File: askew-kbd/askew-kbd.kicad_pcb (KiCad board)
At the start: 2 copper layers, 166.1 x 111 mm, 45 parts, among them SW1 SW_PUSH, SW10 SW_PUSH, SW11 SW_PUSH, SW12 SW_PUSH, SW13 SW_PUSH, SW14 SW_PUSH, SW15 SW_PUSH, SW16 SW_PUSH, SW17 SW_PUSH, SW18 SW_PUSH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

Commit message: unrouted base
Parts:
- U1: footprint kbd:ProMicro_v2 -> keyboard_reversible:ProMicro_unrouted
- moved D22 9.83 mm to (192.2, 137.8), turned to 60 degrees
- moved U1 1.35 mm to (205.0, 79.6), turned to -95 degrees
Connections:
- U1 pad 10: unconnected-(U1-Pad10) -> home
- U1 pad 11: unconnected-(U1-Pad11) -> bottom
- U1 pad 12: unconnected-(U1-Pad12) -> thumb
- U1 pad 21: unconnected-(U1-Pad21) -> VCC
- U1 pad 22: unconnected-(U1-Pad22) -> reset
- U1 pad 23: unconnected-(U1-Pad23) -> GND
- U1 pad 3: unconnected-(U1-Pad3) -> GND
- U1 pad 4: unconnected-(U1-Pad4) -> GND
- U1 pad 9: unconnected-(U1-Pad9) -> top
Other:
- board size 166.1 x 111 mm -> 157.1 x 109 mm

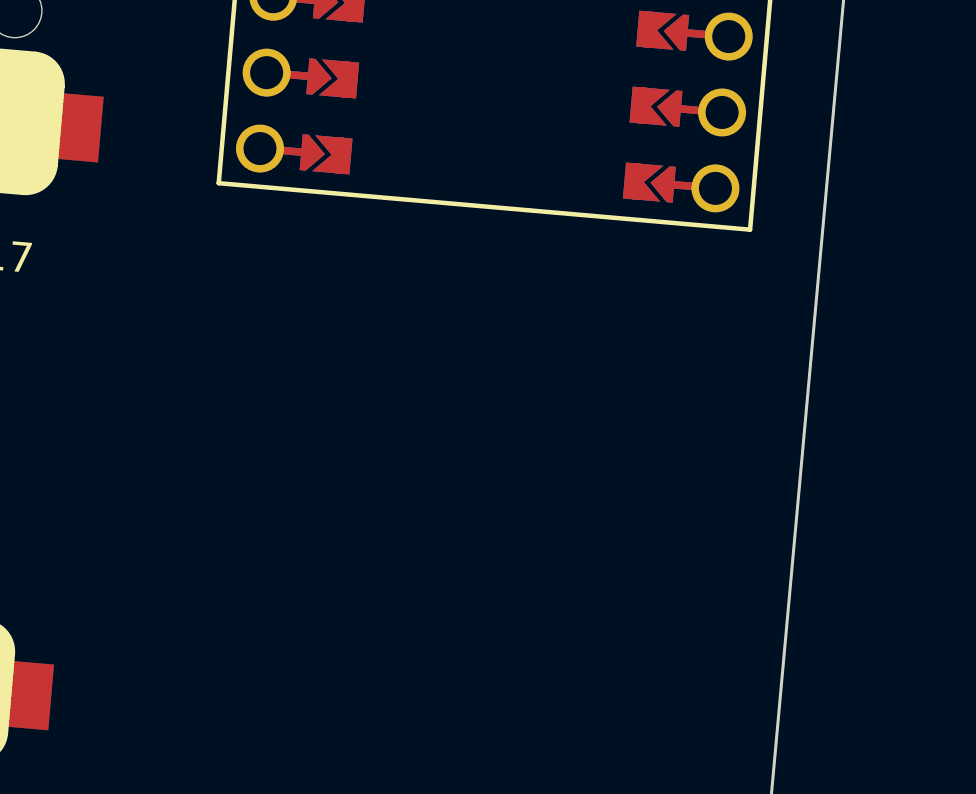
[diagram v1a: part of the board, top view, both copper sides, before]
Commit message: trrs and reset switch
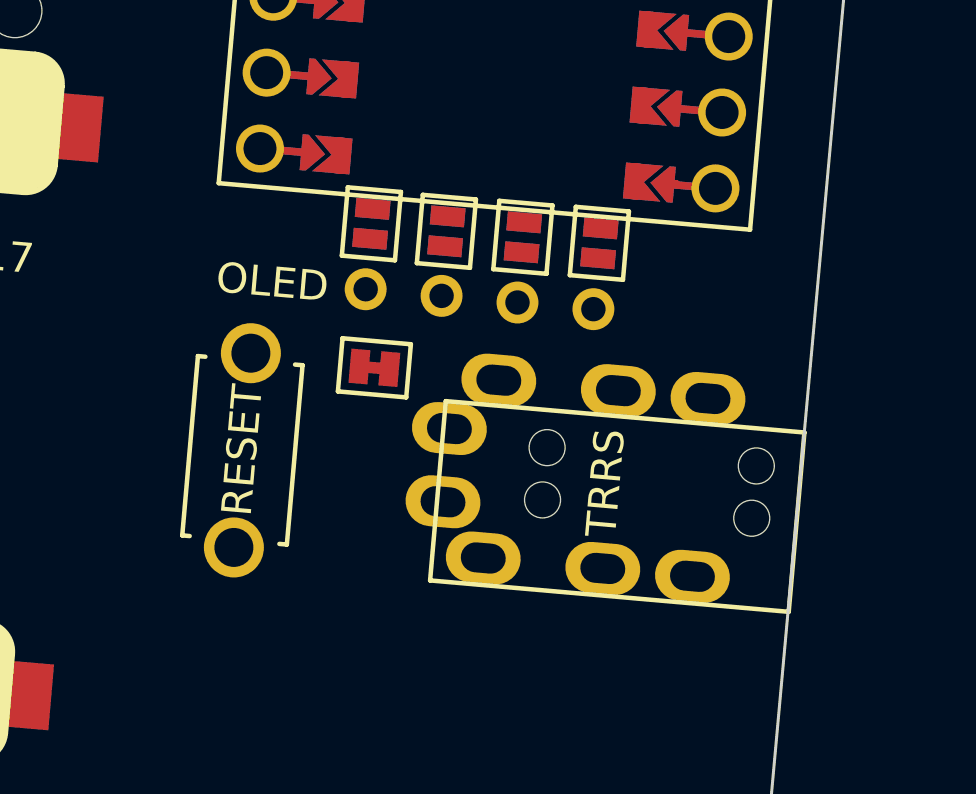
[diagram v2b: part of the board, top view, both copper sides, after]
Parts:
- added J1: OLED, kbd:OLED_v2, F.Cu at (203.5, 97.9)
- added J2: MJ-4PP-9, kbd:MJ-4PP-9, F.Cu at (214.1, 105.3)
- added JP1: , kbd:Jumper, F.Cu at (207.5, 96.0)
- added JP2: , kbd:Jumper, F.Cu at (204.9, 95.8)
- added JP3: , kbd:Jumper, F.Cu at (202.4, 95.6)
- added JP4: , kbd:Jumper, F.Cu at (199.9, 95.3)
- added JP5: , kbd:Jumper, B.Cu at (207.5, 96.0)
- added JP6: , kbd:Jumper, B.Cu at (204.9, 95.8)
- added JP7: , kbd:Jumper, B.Cu at (202.4, 95.6)
- added JP8: , kbd:Jumper, B.Cu at (199.9, 95.3)
- added JP9: , kbd:JPC2, F.Cu at (200.0, 100.2)
- added RSW1: SW_PUSH, kbd:ResetSW, F.Cu at (195.6, 102.9)
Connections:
- U1 pad 2: unconnected-(U1-Pad2) -> data
- U1 pad 5: unconnected-(U1-Pad5) -> SDA
- U1 pad 6: unconnected-(U1-Pad6) -> SCL
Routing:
- net (no net): track 0.00 -> 0.52 mm

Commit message: outline
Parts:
- added REF**: M2_Hole_TH, kbd:M2_Hole_TH, F.Cu at (205.2, 122.6)
- added REF**: M2_Hole_TH, kbd:M2_Hole_TH, F.Cu at (194.5, 114.5)
- added Ref**: Val**, kbd:M2_HOLE, F.Cu at (136.2, 130.5)
- added Ref**: Val**, kbd:M2_HOLE, F.Cu at (90.2, 104.7)
- added Ref**: Val**, kbd:M2_HOLE, F.Cu at (189.9, 122.8)
- added Ref**: Val**, kbd:M2_HOLE, F.Cu at (152.0, 71.0)
- added Ref**: Val**, kbd:M2_HOLE, F.Cu at (151.8, 98.1)
- added Ref**: Val**, kbd:M2_HOLE, F.Cu at (85.3, 86.2)
- added Ref**: Val**, kbd:M2_HOLE, F.Cu at (105.5, 73.2)
- moved JP9 9.04 mm to (208.4, 96.8), turned to 175 degrees
- moved J2 3.27 mm to (210.8, 104.9)
- moved RSW1 1.83 mm to (193.8, 102.5)
- moved J1 1.71 mm to (201.8, 97.7)
- moved JP1 1.71 mm to (205.8, 95.8)
- moved JP3 1.71 mm to (200.7, 95.4)
- moved JP4 1.71 mm to (198.2, 95.2)
- moved JP5 1.71 mm to (205.8, 95.8)
- moved JP7 1.71 mm to (200.7, 95.4)
- moved JP8 1.71 mm to (198.2, 95.2)
- moved JP2 1.71 mm to (203.3, 95.6)
- moved JP6 1.71 mm to (203.3, 95.6)
- moved U1 1.71 mm to (203.3, 79.4)
- moved D1 1.17 mm to (65.6, 80.7)
- moved D2 1.17 mm to (70.5, 99.1)
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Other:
- board size 157.1 x 109 mm -> 155.6 x 108.4 mm

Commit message: add breadcrumbs for far pinky
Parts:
- added Ref**: Val**, kbd:M2_HOLE, F.Cu at (110.2, 91.9)
- moved Ref** 9.97 mm to (153.6, 80.8)
- moved Ref** 3.25 mm to (108.8, 73.3)
- moved Ref** 1.74 mm to (152.7, 99.6)
- moved Ref** 0.06 mm to (85.2, 86.2)
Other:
- outline, holes or cut-outs redrawn

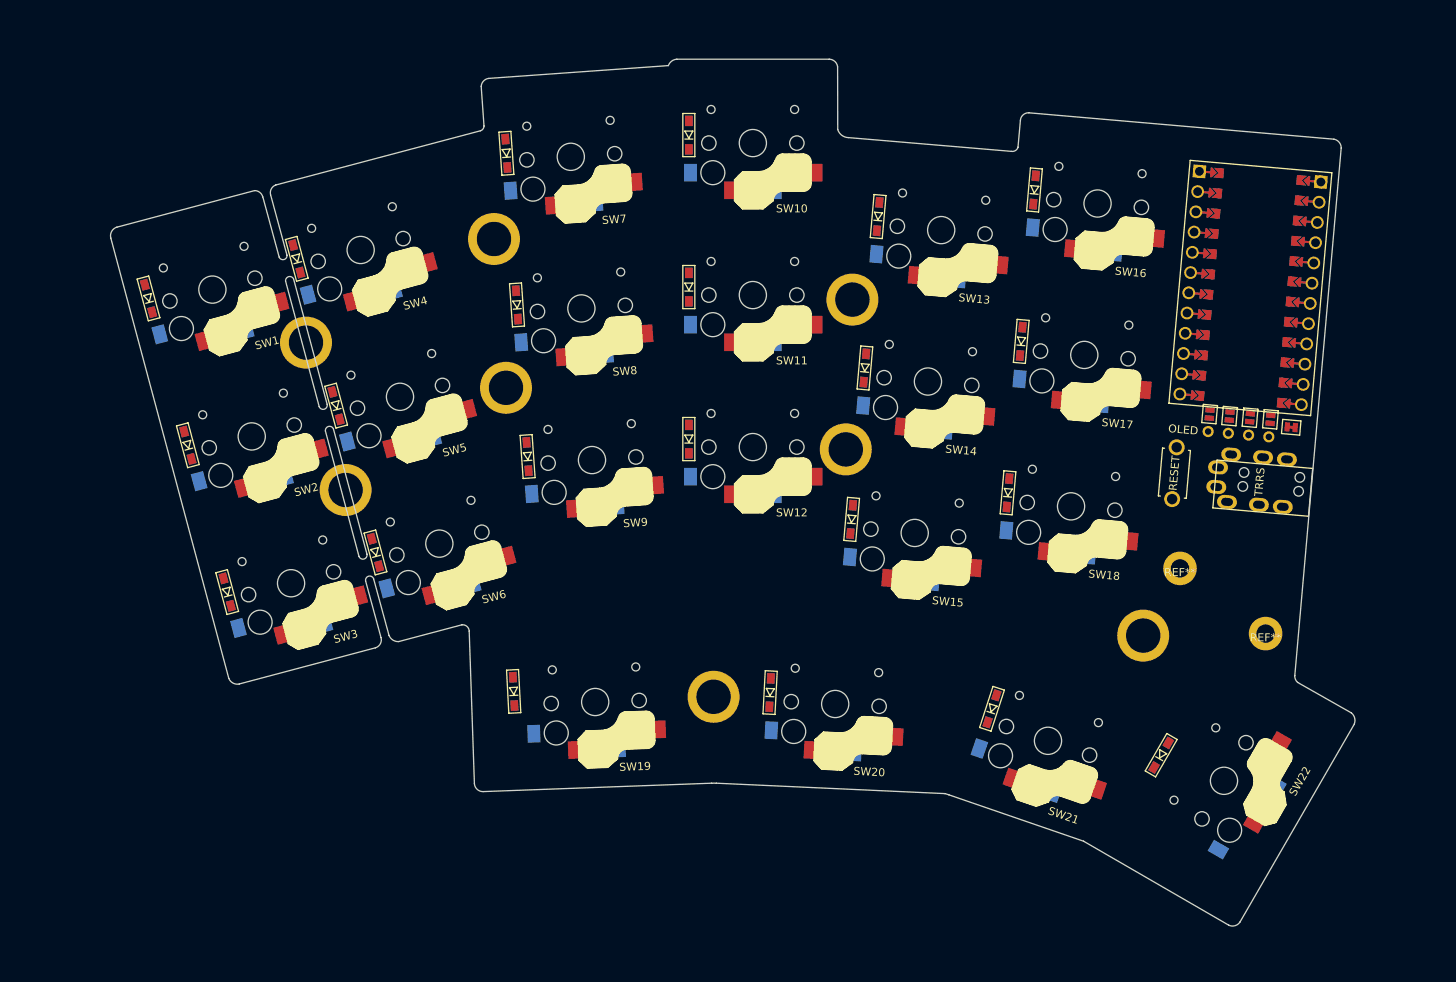
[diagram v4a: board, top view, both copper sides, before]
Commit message: mounting holes
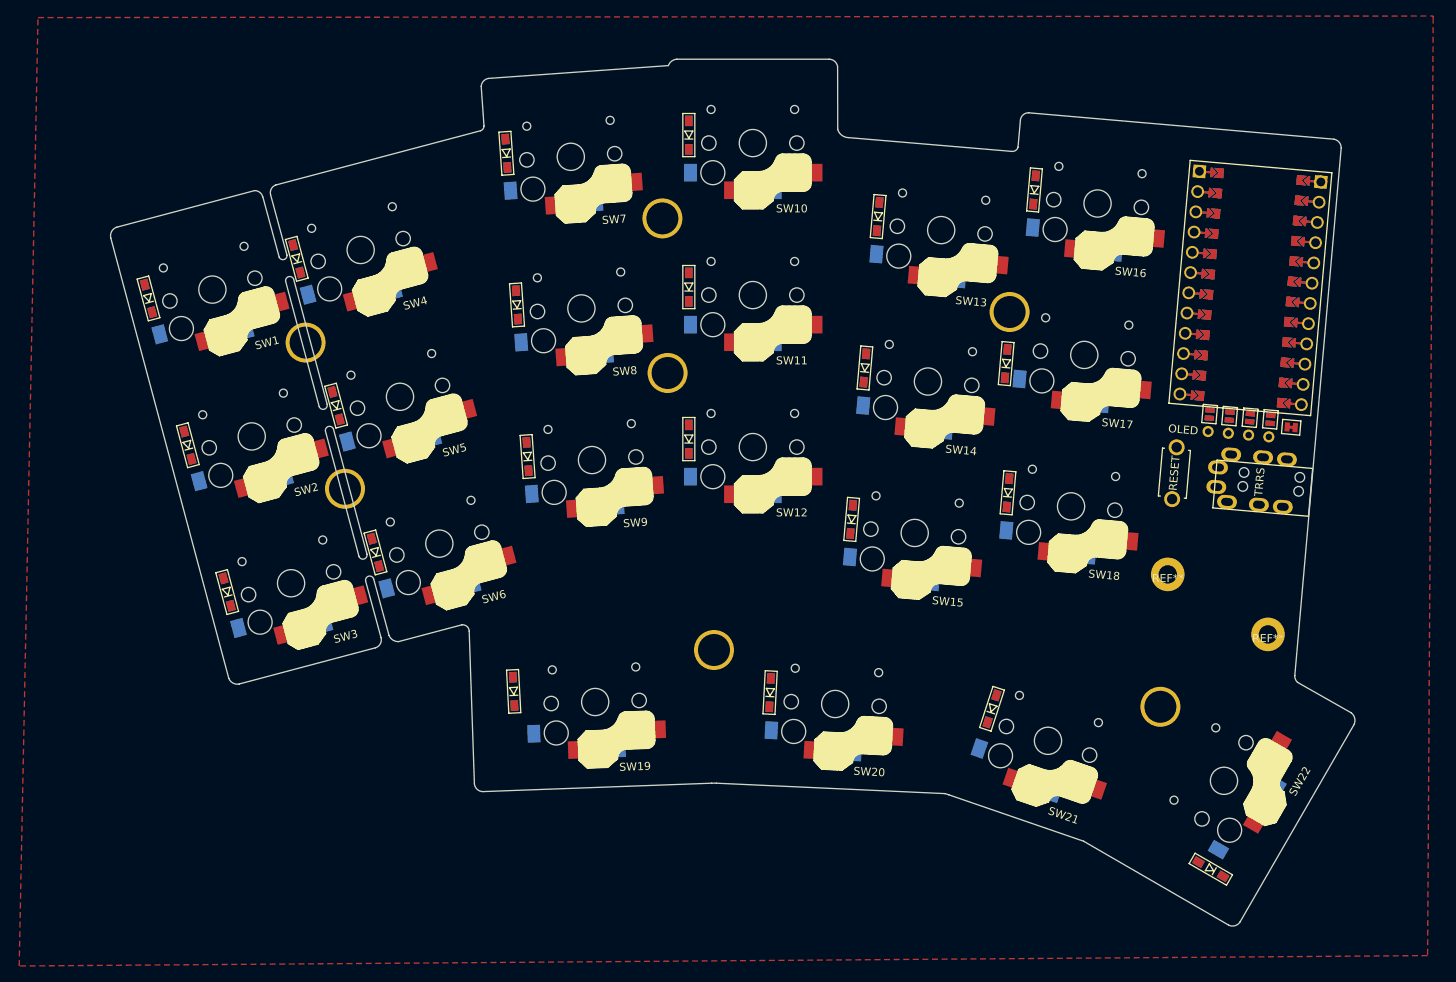
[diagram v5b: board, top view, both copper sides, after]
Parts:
- removed the REF** at (205.2, 122.6)
- removed the REF** at (194.5, 114.5)
- removed Ref** (x8): Val**, kbd:M2_HOLE
- added REF**: M2_Hole_TH_Outside, kbd:M2_Hole_TH_Outside, F.Cu at (192.1, 131.8)
- added REF**: M2_Hole_TH_Outside, kbd:M2_Hole_TH_Outside, F.Cu at (130.4, 90.0)
- added REF**: M2_Hole_TH_Outside, kbd:M2_Hole_TH_Outside, F.Cu at (136.2, 124.7)
- added REF**: M2_Hole_TH, kbd:M2_Hole_TH, F.Cu at (193.0, 115.2)
- added REF**: M2_Hole_TH_Outside, kbd:M2_Hole_TH_Outside, F.Cu at (129.8, 70.7)
- added REF**: M2_Hole_TH, kbd:M2_Hole_TH, F.Cu at (205.5, 122.7)
- added REF**: M2_Hole_TH_Outside, kbd:M2_Hole_TH_Outside, F.Cu at (173.2, 82.4)
- added REF**: M2_Hole_TH_Outside, kbd:M2_Hole_TH_Outside, F.Cu at (90.1, 104.5)
- added REF**: M2_Hole_TH_Outside, kbd:M2_Hole_TH_Outside, F.Cu at (85.2, 86.2)
- moved D22 15.5 mm to (198.3, 152.1), turned to 150 degrees
- moved D17 3.35 mm to (172.8, 88.8)
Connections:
- U1 pad 1: unconnected-(U1-Pad1) -> LED
- U1 pad 13: unconnected-(U1-Pad13) -> col0
- U1 pad 14: unconnected-(U1-Pad14) -> col1
- U1 pad 15: unconnected-(U1-Pad15) -> col2
- U1 pad 16: unconnected-(U1-Pad16) -> col3
- U1 pad 17: unconnected-(U1-Pad17) -> col4
- U1 pad 18: unconnected-(U1-Pad18) -> col5
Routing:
- added copper zone on F.Cu, net GND

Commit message: buzzer
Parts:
- added BZ1: Buzzer, Buzzer_Beeper:Buzzer_12x9.5RM7.6, F.Cu at (198.7, 113.7)
- added JP10: , kbd:Jumper, F.Cu at (196.9, 106.8)
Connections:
- U1 pad 8: unconnected-(U1-Pad8) -> buzzer
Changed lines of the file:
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@@
   (net 2 "unconnected-(U1-Pad20)")
   (net 3 "unconnected-(U1-Pad19)")
-  (net 4 "unconnected-(U1-Pad8)")
+  (net 4 "buzzer")
   (net 5 "unconnected-(U1-Pad7)")
   (net 6 "Net-(D1-Pad1)")
@@
   (net 48 "Net-(J2-PadC)")
   (net 49 "LED")
+  (net 50 "Net-(BZ1-Pad1)")
   (footprint "kbd:D3_SMD" (layer "F.Cu")
     (at 172.775 88.85 85)
@@
     (property "Spice_Primitive" "D")
     (autoplace_cost180 10)
-    (attr through_hole)
+    (attr smd)
     (fp_text reference "D17" (at 0.5 0 85) (layer "F.Fab") hide
       (effects (font (size 0.5 0.5) (thickness 0.125)))
@@
       (net 32 "bottom") (pinfunction "K") (pintype "passive"))
     (model "Diodes_SMD.3dshapes/SMB_Handsoldering.wrl"
-      (offset (xyz 0 0 0))
+      (offset (xyz -0.5 0 0))
       (scale (xyz 0.22 0.15 0.15))
       (rotate (xyz 0 0 180))
@@
     )
   )
+  (footprint "Buzzer_Beeper:Buzzer_12x9.5RM7.6" (layer "F.Cu")
+    (at 198.689365 113.720987 -5)
+    (descr "Generic Buzzer, D12mm height 9.5mm with RM7.6mm")
+    (tags "buzzer")
+    (property "Sheetfile" "askew-kbd.kicad_sch")
+    (property "Sheetname" "")
+    (attr through_hole)
+    (fp_text reference "BZ1" (at 3.8 -2.5 -5 unlocked) (layer "F.SilkS")
+      (effects (font (size 1 1) (thickness 0.15)))
+    )
+    (fp_text value "Buzzer" (at 3.8 7.4 175) (layer "F.Fab") hide
+      (effects (font (size 1 1) (thickness 0.15)))
+    )
+    (fp_text user "${REFERENCE}" (at 3.702182 -2.55337 -5 unlocked) (layer "B.SilkS")
+      (effects (font (size 1 1) (thickness 0.15)) (justify mirror))
+    )
+    (fp_text user "+" (at 7.56 -2.54 175) (layer "B.SilkS")
+      (effects (font (size 1 1) (thickness 0.15)) (justify mirror))
+    )
+    (fp_text user "+" (at -0.01 -2.54 175) (layer "F.SilkS")
+      (effects (font (size 1 1) (thickness 0.15)))
+    )
+    (fp_text user "+" (at 7.56 -2.54 175) (layer "B.Fab") hide
+      (effects (font (size 1 1) (thickness 0.15)) (justify mirror))
+    )
+    (fp_text user "${REFERENCE}" (at 3.75 -4 175) (layer "B.Fab") hide
+      (effects (font (size 1 1) (thickness 0.15)) (justify mirror))
+    )
+    (fp_text user "${REFERENCE}" (at 3.8 -4 175) (layer "F.Fab") hide
+      (effects (font (size 1 1) (thickness 0.15)))
+    )
+    (fp_text user "+" (at -0.01 -2.54 175) (layer "F.Fab") hide
+      (effects (font (size 1 1) (thickness 0.15)))
+    )
+    (fp_circle (center 3.75 0) (end -2.35 0) (layer "B.SilkS") (width 0.12) (fill none))
+    (fp_circle (center 3.8 0) (end 9.9 0) (layer "F.SilkS") (width 0.12) (fill none))
+    (fp_circle (center 3.75 0) (end -2.5 0) (layer "B.CrtYd") (width 0.05) (fill none))
+    (fp_circle (center 3.8 0) (end 10.05 0) (layer "F.CrtYd") (width 0.05) (fill none))
+    (fp_circle (center 3.75 0) (end 2.75 0) (layer "B.Fab") (width 0.1) (fill none))
+    (fp_circle (center 3.75 0) (end -2.25 0) (layer "B.Fab") (width 0.1) (fill none))
+    (fp_circle (center 3.8 0) (end 9.8 0) (layer "F.Fab") (width 0.1) (fill none))
+    (fp_circle (center 3.8 0) (end 4.8 0) (layer "F.Fab") (width 0.1) (fill none))
+    (pad "1" thru_hole rect (at 0 0 355) (size 2 2) (drill 1) (layers *.Cu *.Mask)
+      (net 50 "Net-(BZ1-Pad1)") (pinfunction "-") (pintype "passive"))
+    (pad "2" thru_hole circle (at 7.6 0 355) (size 2 2) (drill 1) (layers *.Cu *.Mask)
+      (net 38 "GND") (pinfunction "+") (pintype "passive"))
+    (model "${KICAD6_3DMODEL_DIR}/Buzzer_Beeper.3dshapes/Buzzer_12x9.5RM7.6.wrl"
+      (offset (xyz 0 0 0))
+      (scale (xyz 1 1 1))
+      (rotate (xyz 0 0 0))
+    )
+  )
   (footprint "kbd:M2_Hole_TH_Outside" (layer "F.Cu")
     (at 129.8 70.7)
@@
     )
   )
+  (footprint "kbd:Jumper" (layer "F.Cu")
+    (at 196.9 106.75 85)
+    (property "Sheetfile" "askew-kbd.kicad_sch")
+    (property "Sheetname" "")
+    (attr smd)
+    (fp_text reference "JP10" (at -2.413 0.127 85) (layer "F.SilkS") hide
+      (effects (font (size 0.8128 0.8128) (thickness 0.1524)))
+    )
+    (fp_text value " " (at -2.794 0 85) (layer "F.SilkS")
+      (effects (font (size 0.8128 0.8128) (thickness 0.15)))
+    )
+    (fp_line (start 1.143 0.889) (end -1.143 0.889) (layer "F.SilkS") (width 0.15))
+    (fp_line (start 1.143 -0.889) (end 1.143 0.889) (layer "F.SilkS") (width 0.15))
+    (fp_line (start -1.143 -0.889) (end 1.143 -0.889) (layer "F.SilkS") (width 0.15))
+    (fp_line (start -1.143 0.889) (end -1.143 -0.889) (layer "F.SilkS") (width 0.15))
+    (pad "1" smd rect locked (at -0.50038 0 85) (size 0.635 1.143) (layers "F.Cu" "F.Paste" "F.Mask")
+      (net 50 "Net-(BZ1-Pad1)") (pinfunction "1") (pintype "passive") (clearance 0.1905))
+    (pad "2" smd rect locked (at 0.50038 0 85) (size 0.635 1.143) (layers "F.Cu" "F.Paste" "F.Mask")
+      (net 4 "buzzer") (pinfunction "2") (pintype "passive") (clearance 0.1905))
+    (model "smd\\resistors\\R0603.wrl"
+      (offset (xyz 0 0 0.02539999962))
+      (scale (xyz 0.5 0.5 0.5))
+      (rotate (xyz 0 0 0))
+    )
+  )
   (footprint "fp:ChocV1_V2_Hotswap_reversed_15u" locked (layer "F.Cu")
     (at 151.4 131.4 -3)
@@
       ))
     (pad "8" smd custom locked (at 3.81 -4.826 265) (size 1.2 0.5) (layers "F.Cu" "F.Mask")
-      (net 4 "unconnected-(U1-Pad8)") (pinfunction "5/C6") (pintype "bidirectional") (clearance 0.1) (zone_connect 0)
+      (net 4 "buzzer") (pinfunction "5/C6") (pintype "bidirectional") (clearance 0.1) (zone_connect 0)
       (options (clearance outline) (anchor rect))
       (primitives
@@
       ))
     (pad "8" smd custom locked (at 3.81 4.826 85) (size 1.2 0.5) (layers "B.Cu" "B.Mask")
-      (net 4 "unconnected-(U1-Pad8)") (pinfunction "5/C6") (pintype "bidirectional") (clearance 0.1) (zone_connect 0)
+      (net 4 "buzzer") (pinfunction "5/C6") (pintype "bidirectional") (clearance 0.1) (zone_connect 0)
       (options (clearance outline) (anchor rect))
       (primitives
